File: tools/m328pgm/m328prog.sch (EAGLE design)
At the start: 11 parts, among them J1 AVR_SPI_PROG_3X2PTH, U1 ATMEGA328P

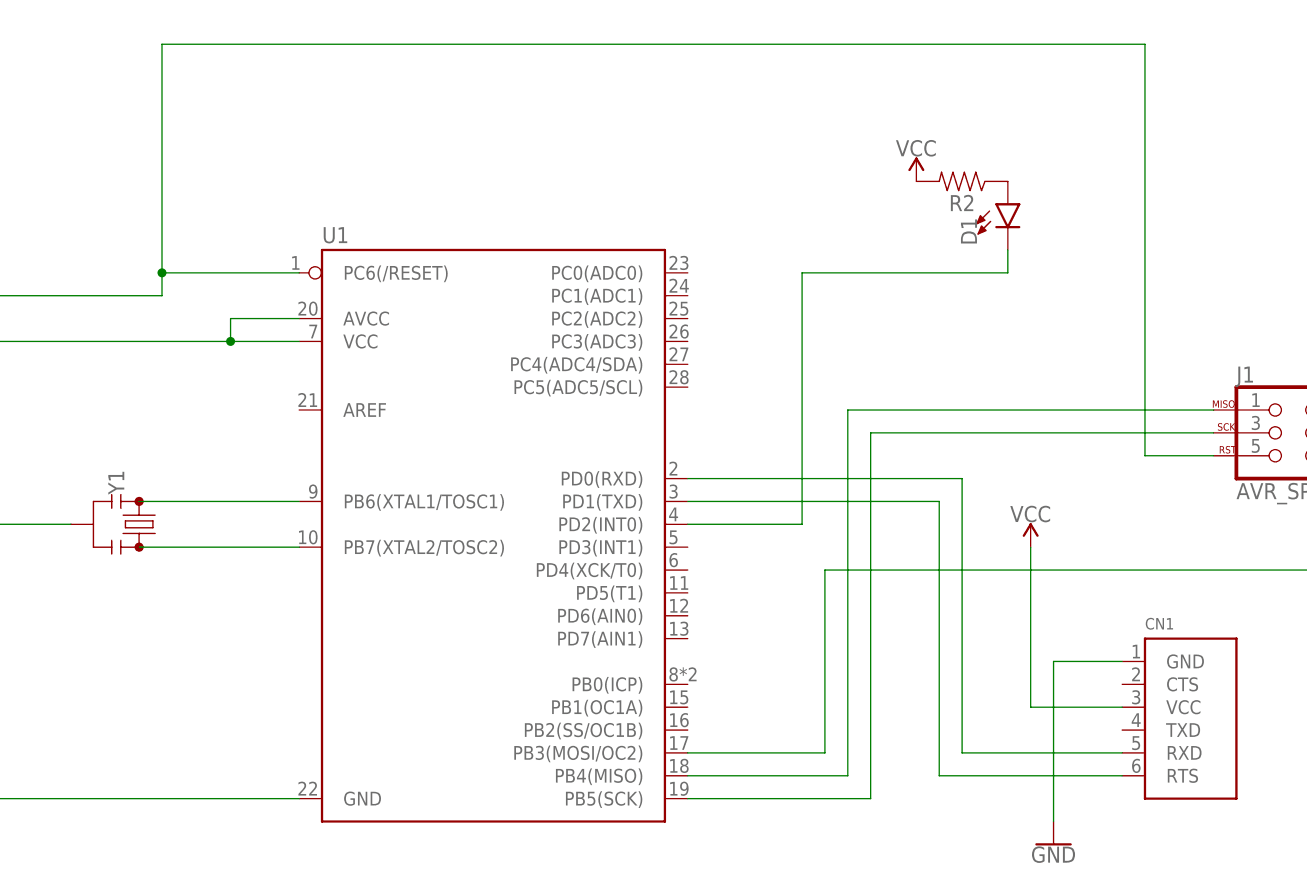
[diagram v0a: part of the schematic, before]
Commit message: Update several tool boards.
+ AEPRO had the wrong socket size; the ZIF footprint was for
  a narrow 28-pin DIP.
+ AEPRO was missing an inverter on the LEDs.
+ M328PGM had a serial line tied to RST: any attempt at using the
  UART caused the board to reset.
+ M1284PGM had no silkscreen markings to identify the board.
+ M1284PGM had no decoupling capacitor for the MCU.
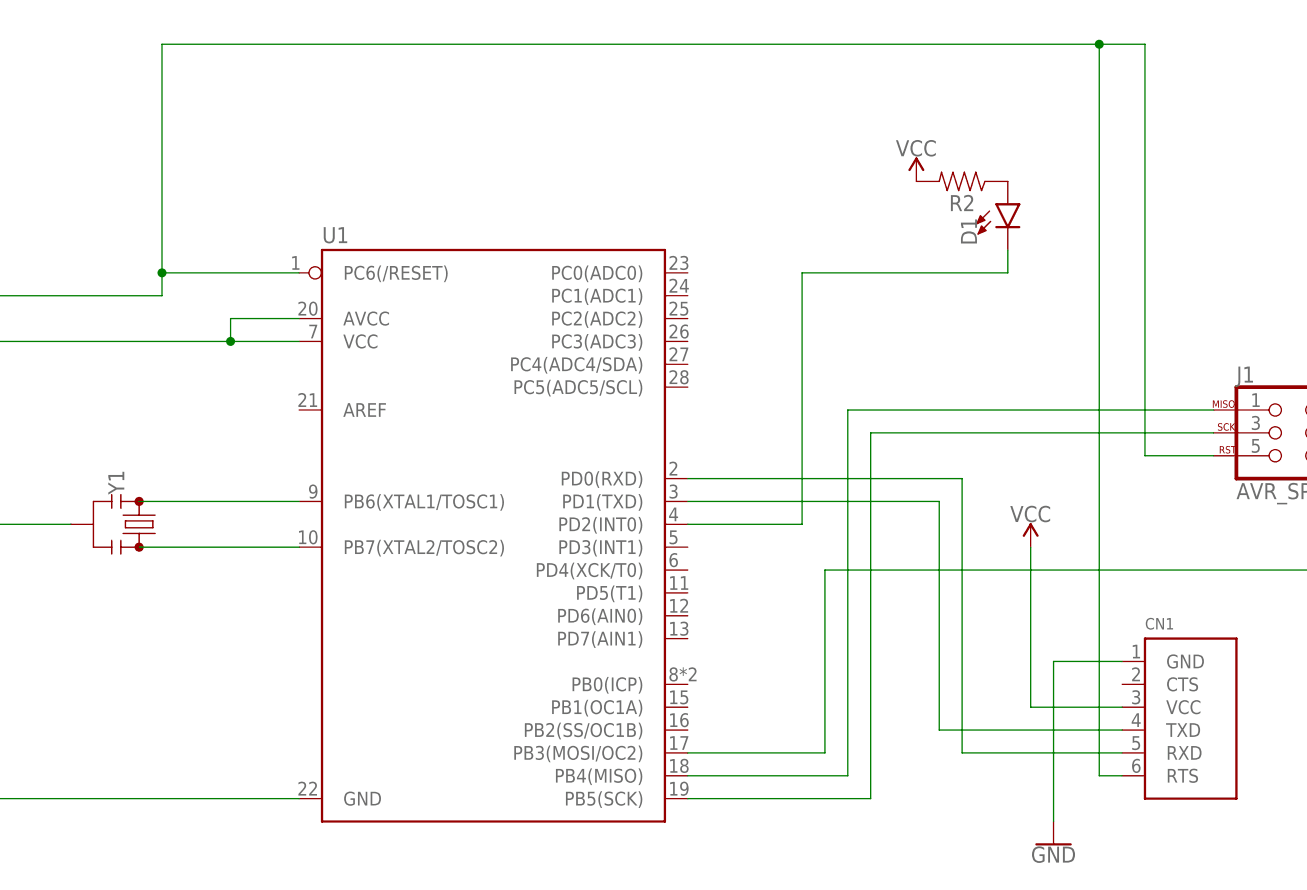
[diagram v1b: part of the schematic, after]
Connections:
- net N$10: now also CN1.TXD; no longer CN1.RTS
- net N$4: now also CN1.RTS
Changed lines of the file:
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@@
 <drawing>
 <settings>
-<setting alwaysvectorfont="yes"/>
+<setting alwaysvectorfont="no"/>
 <setting verticaltext="up"/>
 </settings>
@@
 <junction x="-33.02" y="38.1"/>
 <wire x1="7.62" y1="40.64" x2="7.62" y2="66.04" width="0.1524" layer="91"/>
-<wire x1="7.62" y1="66.04" x2="116.84" y2="66.04" width="0.1524" layer="91"/>
+<wire x1="7.62" y1="66.04" x2="111.76" y2="66.04" width="0.1524" layer="91"/>
 <pinref part="J1" gate="G$1" pin="5"/>
+<wire x1="111.76" y1="66.04" x2="116.84" y2="66.04" width="0.1524" layer="91"/>
 <wire x1="116.84" y1="66.04" x2="116.84" y2="20.32" width="0.1524" layer="91"/>
 <wire x1="116.84" y1="20.32" x2="124.46" y2="20.32" width="0.1524" layer="91"/>
@@
 <wire x1="7.62" y1="38.1" x2="7.62" y2="40.64" width="0.1524" layer="91"/>
 <junction x="7.62" y="40.64"/>
+<pinref part="CN1" gate="G$1" pin="RTS"/>
+<wire x1="114.3" y1="-15.24" x2="111.76" y2="-15.24" width="0.1524" layer="91"/>
+<wire x1="111.76" y1="-15.24" x2="111.76" y2="66.04" width="0.1524" layer="91"/>
+<junction x="111.76" y="66.04"/>
 </segment>
 </net>
@@
 <pinref part="U1" gate="G$1" pin="PD1(TXD)"/>
 <wire x1="66.04" y1="15.24" x2="93.98" y2="15.24" width="0.1524" layer="91"/>
-<wire x1="93.98" y1="15.24" x2="93.98" y2="-15.24" width="0.1524" layer="91"/>
-<wire x1="93.98" y1="-15.24" x2="114.3" y2="-15.24" width="0.1524" layer="91"/>
-<pinref part="CN1" gate="G$1" pin="RTS"/>
-</segment>
-</net>
+<pinref part="CN1" gate="G$1" pin="TXD"/>
+<wire x1="114.3" y1="-10.16" x2="93.98" y2="-10.16" width="0.1524" layer="91"/>
+<wire x1="93.98" y1="-10.16" x2="93.98" y2="15.24" width="0.1524" layer="91"/>
+</segment>
+</net>

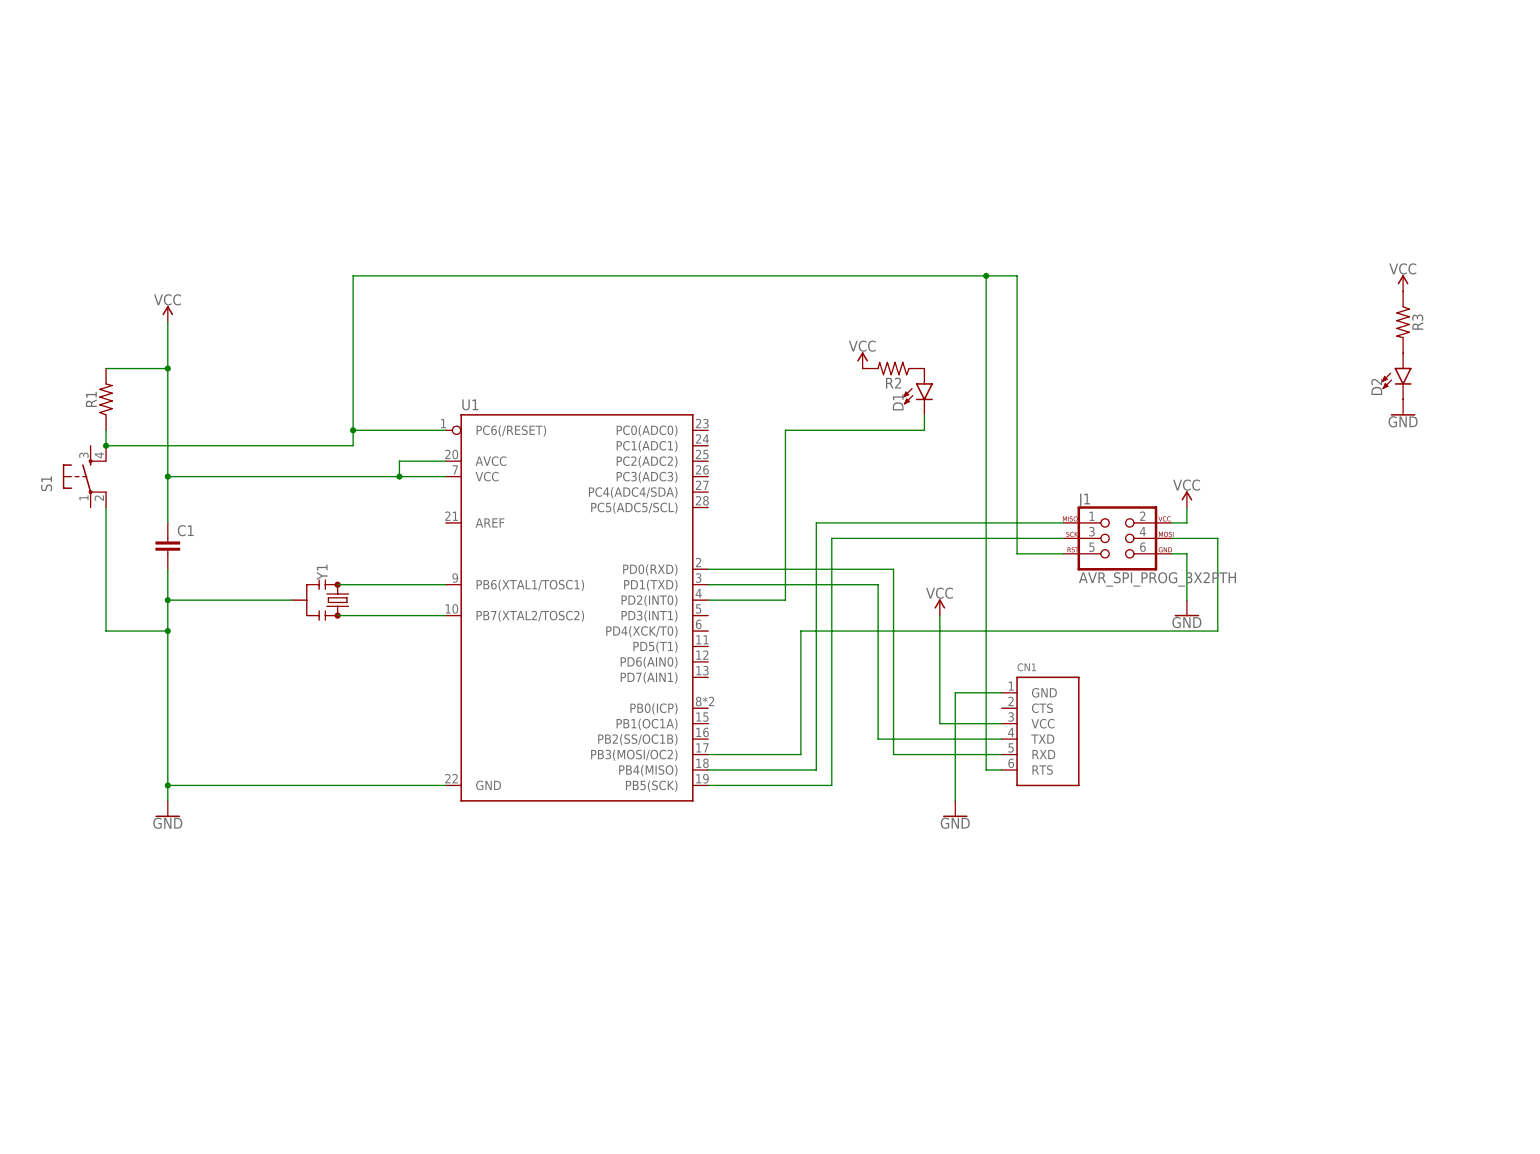
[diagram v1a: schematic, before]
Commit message: Fix UART issues in programmers.
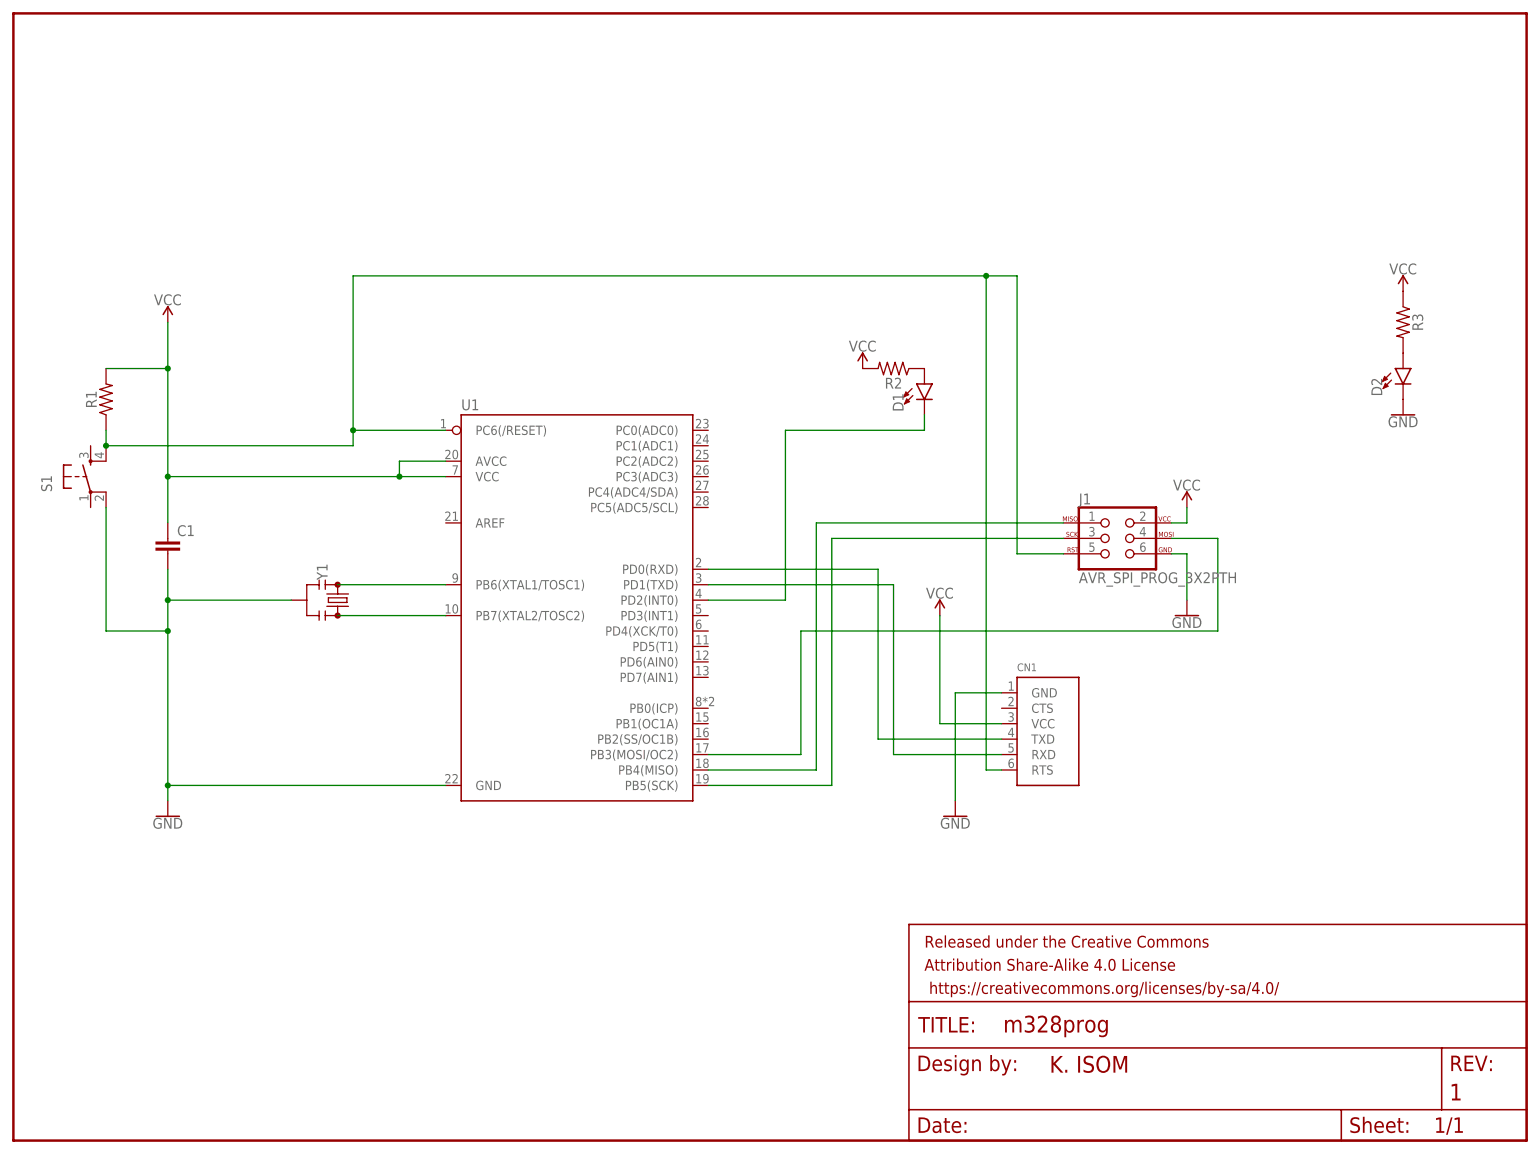
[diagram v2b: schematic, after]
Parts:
- added FRAME1: FRAME-LETTER, SparkFun-Aesthetics:FRAME-LETTER
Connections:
- net N$10: now also U1.PD0(RXD); no longer U1.PD1(TXD)
- net N$9: now also U1.PD1(TXD); no longer U1.PD0(RXD)
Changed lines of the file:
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@@
 <drawing>
 <settings>
-<setting alwaysvectorfont="no"/>
+<setting alwaysvectorfont="yes"/>
 <setting verticaltext="up"/>
 </settings>
@@
 <schematic xreflabel="%F%N/%S.%C%R" xrefpart="/%S.%C%R">
 <attributes>
+<attribute name="DESIGNER" value="K. ISOM"/>
 </attributes>
 <variantdefs>
@@
 <part name="GND3" library="SparkFun-PowerSymbols" deviceset="GND" device=""/>
 <part name="SUPPLY3" library="SparkFun-PowerSymbols" deviceset="VCC" device=""/>
+<part name="FRAME1" library="SparkFun-Aesthetics" deviceset="FRAME-LETTER" device="">
+<attribute name="DESIGNER" value="K. ISOM"/>
+<attribute name="REV" value="1"/>
+</part>
 </parts>
 <sheets>
@@
 <instance part="SUPPLY3" gate="G$1" x="104.14" y="10.16" smashed="yes">
 <attribute name="VALUE" x="104.14" y="12.954" size="1.778" layer="96" align="bottom-center"/>
+</instance>
+<instance part="FRAME1" gate="G$1" x="-48.26" y="-76.2" smashed="yes"/>
+<instance part="FRAME1" gate="V" x="99.06" y="-76.2" smashed="yes">
+<attribute name="LAST_DATE_TIME" x="111.76" y="-74.93" size="2.54" layer="94" font="vector"/>
+<attribute name="SHEET" x="185.42" y="-74.93" size="2.54" layer="94" font="vector"/>
+<attribute name="DRAWING_NAME" x="114.554" y="-58.42" size="2.7432" layer="94" font="vector"/>
+<attribute name="DESIGNER" x="122.174" y="-65.024" size="2.7432" layer="94" font="vector"/>
+<attribute name="REV" x="187.96" y="-69.596" size="2.7432" layer="94" font="vector"/>
 </instance>
 </instances>
@@
 <net name="N$9" class="0">
 <segment>
-<pinref part="U1" gate="G$1" pin="PD0(RXD)"/>
-<wire x1="66.04" y1="17.78" x2="96.52" y2="17.78" width="0.1524" layer="91"/>
-<wire x1="96.52" y1="17.78" x2="96.52" y2="-12.7" width="0.1524" layer="91"/>
 <pinref part="CN1" gate="G$1" pin="RXD"/>
+<wire x1="96.52" y1="15.24" x2="96.52" y2="-12.7" width="0.1524" layer="91"/>
 <wire x1="96.52" y1="-12.7" x2="114.3" y2="-12.7" width="0.1524" layer="91"/>
+<pinref part="U1" gate="G$1" pin="PD1(TXD)"/>
+<wire x1="66.04" y1="15.24" x2="96.52" y2="15.24" width="0.1524" layer="91"/>
 </segment>
 </net>
 <net name="N$10" class="0">
 <segment>
-<pinref part="U1" gate="G$1" pin="PD1(TXD)"/>
-<wire x1="66.04" y1="15.24" x2="93.98" y2="15.24" width="0.1524" layer="91"/>
 <pinref part="CN1" gate="G$1" pin="TXD"/>
 <wire x1="114.3" y1="-10.16" x2="93.98" y2="-10.16" width="0.1524" layer="91"/>
-<wire x1="93.98" y1="-10.16" x2="93.98" y2="15.24" width="0.1524" layer="91"/>
-</segment>
-</net>
+<wire x1="93.98" y1="-10.16" x2="93.98" y2="17.78" width="0.1524" layer="91"/>
+<pinref part="U1" gate="G$1" pin="PD0(RXD)"/>
+<wire x1="93.98" y1="17.78" x2="66.04" y2="17.78" width="0.1524" layer="91"/>
+</segment>
+</net>
